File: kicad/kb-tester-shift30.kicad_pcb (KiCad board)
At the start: 2 copper layers, 135 x 92 mm, 64 parts, among them J1 Conn_01x12_Pin, J2 Conn_01x05_Socket, J3 8-1437565-1, SW1 PG1350, SW10 PG1350, SW11 PG1350, SW12 PG1350, SW13 PG1350, SW14 PG1350, SW15 PG1350, SW16 PG1350, SW17 PG1350, SW18 PG1350, SW19 PG1350, SW2 PG1350, SW20 PG1350, SW21 PG1350, SW22 PG1350, SW23 PG1350, SW24 PG1350, SW25 PG1350, SW26 PG1350, SW27 PG1350, SW28 PG1350, SW29 PG1350, SW3 PG1350, SW30 PG1350, SW4 PG1350, SW5 PG1350, SW6 PG1350, SW7 PG1350, SW8 PG1350, SW9 PG1350, U2 74HC595

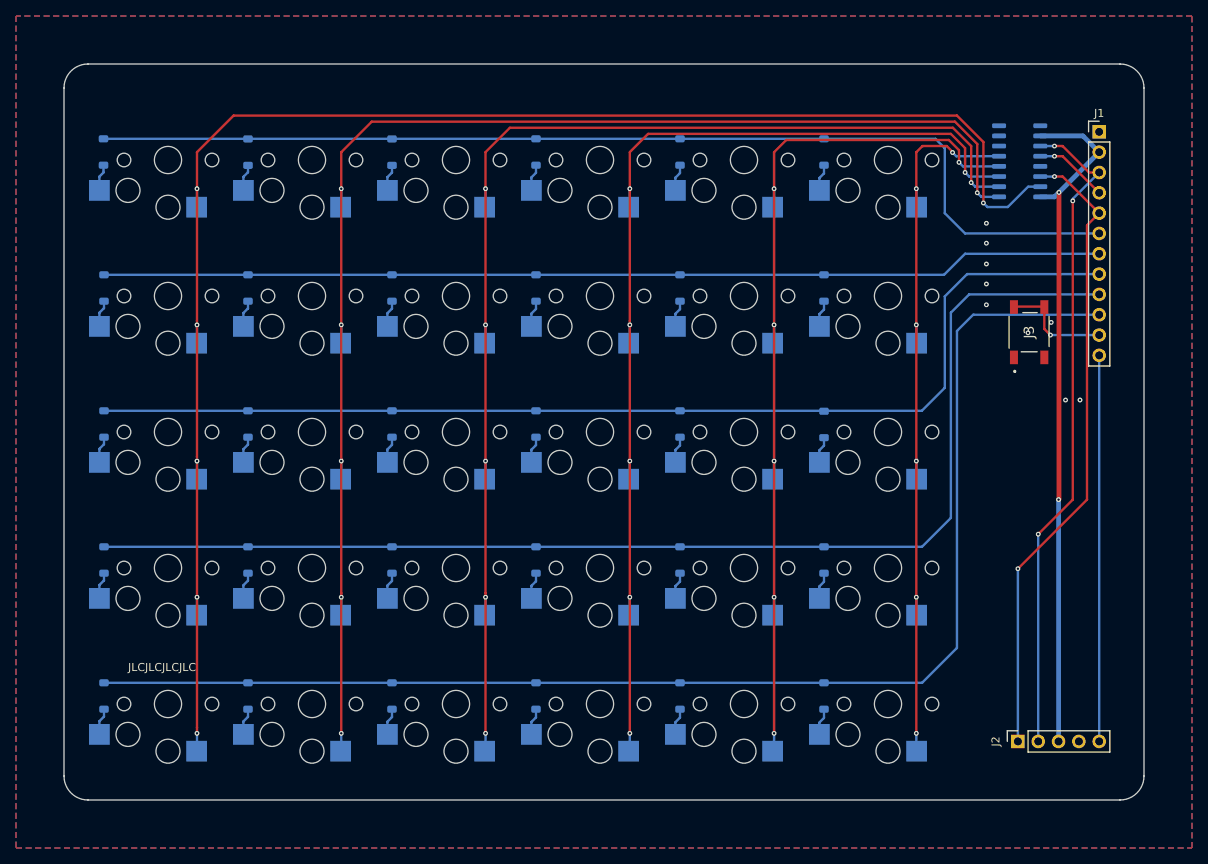
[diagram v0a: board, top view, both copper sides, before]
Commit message: Improved routing
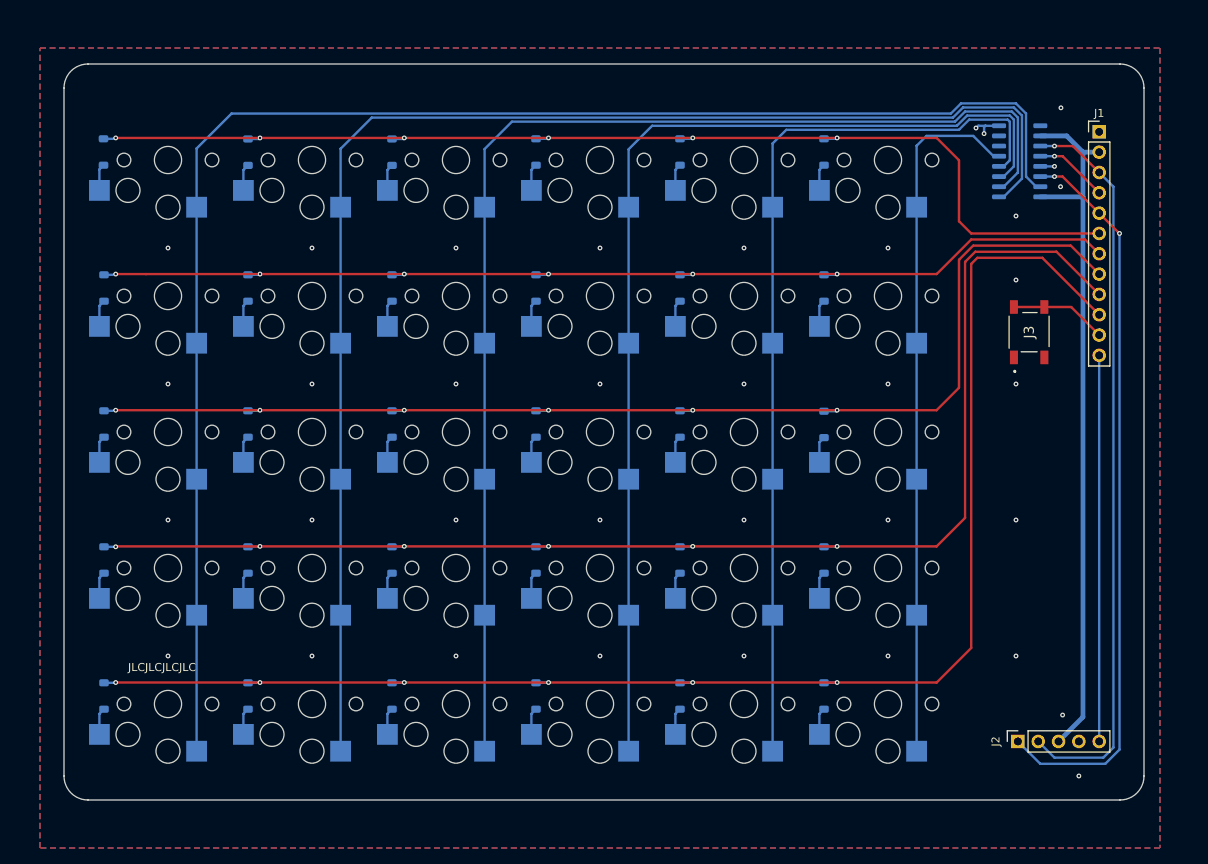
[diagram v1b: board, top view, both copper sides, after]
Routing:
- net ROW5: track 166.7 -> 185.4 mm, vias 0 -> 6
- net ROW4: track 152.5 -> 168.6 mm, vias 0 -> 6
- net ROW3: track 138.2 -> 151.8 mm, vias 0 -> 6
- net MOSI: track 79.5 -> 92.0 mm
- net COL1: track 201.7 -> 192.1 mm, vias 6 -> 0
- net ROW2: track 125.5 -> 135.0 mm, vias 0 -> 6
- net SCK: track 83.0 -> 92.1 mm, vias 3 -> 1
- net ROW1: track 134.1 -> 142.0 mm, vias 0 -> 6
- net COL6: track 95.3 -> 87.5 mm, vias 6 -> 0
- net GND: track 0.00 -> 5.84 mm, vias 9 -> 36
- net COL5: track 115.4 -> 113.4 mm, vias 6 -> 0
- net VCC: track 86.5 -> 88.5 mm, vias 2 -> 0
- net COL4: track 135.4 -> 133.6 mm, vias 6 -> 0
- net RESET: track 13.8 -> 12.1 mm, vias 1 -> 0
- net COL3: track 155.4 -> 154.1 mm, vias 6 -> 0
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
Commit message: Logo
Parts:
- added G***: LOGO, logo:logo_10mm, B.Cu at (141.7, 54.6)
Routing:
- net VCC: track 88.5 -> 86.8 mm
- net DSP_CS: track 48.3 -> 49.1 mm
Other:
- board text added: "REV A 3/24"
- board text added: "github.com/mlilley/kb-tester-shift30"
- board text added: "kb-tester-shift30"

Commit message: Add production
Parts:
- added REF**: Jlcpcb Assembly Tooling Hole, assembly:Jlcpcb Assembly Tooling Hole, F.Cu at (26.4, 110.7)
- added REF**: Jlcpcb Assembly Tooling Hole, assembly:Jlcpcb Assembly Tooling Hole, F.Cu at (154.7, 110.7)
- added REF**: Jlcpcb Assembly Tooling Hole, assembly:Jlcpcb Assembly Tooling Hole, F.Cu at (26.4, 25.1)
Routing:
- net GND: vias 36 -> 40
